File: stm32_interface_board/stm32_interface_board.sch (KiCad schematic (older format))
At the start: 17 parts, among them P1 USB_OTG, P10 CONN_01X03, P11 CONN_01X02, P2 CONN_02X25, P3 CONN_02X25, P4 CONN_01X04, P5 CONN_01X04, P6 CONN_01X04, P7 CONN_01X02, P8 CONN_01X02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

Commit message: Adding build errata to STM32 interface board.
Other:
- note added: "IMPORTANT ERRATA:\nThe connections from P3 pins 25, 27, 29 and 32 are not accurate!!\nThe following modifications were made to the board during assembly:\n\nPin 27 and pin 28 were shorted, as pin 27 is incapable of PWM\nTherefore, pin 28 (i.e. PD6) is to be used for PWM.\n\nPin 30 and pin 32 were shorted, as pin 32 is incapable of PWM\nTherefore, pin 30 (i.e. PD4) is to be used for PWM\n\nPins 25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"
- note added: "STM32 P1"
- note added: "STM32 P2"
- moved on the sheet: C12, C13, U3
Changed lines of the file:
@@
 L +BATT #PWR2
 U 1 1 58BAE894
-P 1500 6050
-F 0 "#PWR2" H 1500 5900 50  0001 C CNN
-F 1 "+BATT" H 1500 6190 50  0000 C CNN
-F 2 "" H 1500 6050 50  0000 C CNN
-F 3 "" H 1500 6050 50  0000 C CNN
-	1    1500 6050
+P 850 7150
+F 0 "#PWR2" H 850 7000 50  0001 C CNN
+F 1 "+BATT" H 850 7290 50  0000 C CNN
+F 2 "" H 850 7150 50  0000 C CNN
+F 3 "" H 850 7150 50  0000 C CNN
+	1    850  7150
 	1    0    0    -1
 $EndComp
@@
 L LF50ABDT-TR U3
 U 1 1 58BB42A6
-P 2750 6150
-F 0 "U3" H 2450 6500 50  0000 L CNN
-F 1 "LF50ABDT-TR" H 2450 6400 50  0000 L CNN
-F 2 "TO_SOT_Packages_SMD:TO-252-2Lead" H 2750 6000 50  0001 L CNN
-F 3 "" H 2750 6300 50  0001 C CNN
-	1    2750 6150
+P 2100 7250
+F 0 "U3" H 1800 7600 50  0000 L CNN
+F 1 "LF50ABDT-TR" H 1800 7500 50  0000 L CNN
+F 2 "TO_SOT_Packages_SMD:TO-252-2Lead" H 2100 7100 50  0001 L CNN
+F 3 "" H 2100 7400 50  0001 C CNN
+	1    2100 7250
 	1    0    0    -1
 $EndComp
@@
 L C C12
 U 1 1 58BB4CB4
-P 1900 6250
-F 0 "C12" H 1925 6350 50  0000 L CNN
-F 1 "0.1 uF" H 1925 6150 50  0000 L CNN
-F 2 "Capacitors_SMD:C_0603_HandSoldering" H 1938 6100 50  0001 C CNN
-F 3 "" H 1900 6250 50  0000 C CNN
-F 4 "CC0603KRX7R8BB104" H 1900 6250 60  0001 C CNN "manf#"
-	1    1900 6250
+P 1250 7350
+F 0 "C12" H 1275 7450 50  0000 L CNN
+F 1 "0.1 uF" H 1275 7250 50  0000 L CNN
+F 2 "Capacitors_SMD:C_0603_HandSoldering" H 1288 7200 50  0001 C CNN
+F 3 "" H 1250 7350 50  0000 C CNN
+F 4 "CC0603KRX7R8BB104" H 1250 7350 60  0001 C CNN "manf#"
+	1    1250 7350
 	1    0    0    -1
 $EndComp
@@
 L Earth #PWR5
 U 1 1 58BB5537
-P 1900 6500
-F 0 "#PWR5" H 1900 6250 50  0001 C CNN
-F 1 "Earth" H 1900 6350 50  0001 C CNN
-F 2 "" H 1900 6500 50  0000 C CNN
-F 3 "" H 1900 6500 50  0000 C CNN
-	1    1900 6500
+P 1250 7600
+F 0 "#PWR5" H 1250 7350 50  0001 C CNN
+F 1 "Earth" H 1250 7450 50  0001 C CNN
+F 2 "" H 1250 7600 50  0000 C CNN
+F 3 "" H 1250 7600 50  0000 C CNN
+	1    1250 7600
 	1    0    0    -1
 $EndComp
@@
 L Earth #PWR8
 U 1 1 58BB56DD
-P 2750 6500
-F 0 "#PWR8" H 2750 6250 50  0001 C CNN
-F 1 "Earth" H 2750 6350 50  0001 C CNN
-F 2 "" H 2750 6500 50  0000 C CNN
-F 3 "" H 2750 6500 50  0000 C CNN
-	1    2750 6500
+P 2100 7600
+F 0 "#PWR8" H 2100 7350 50  0001 C CNN
+F 1 "Earth" H 2100 7450 50  0001 C CNN
+F 2 "" H 2100 7600 50  0000 C CNN
+F 3 "" H 2100 7600 50  0000 C CNN
+	1    2100 7600
 	1    0    0    -1
 $EndComp
@@
 L Earth #PWR9
 U 1 1 58BB5950
-P 3400 6500
-F 0 "#PWR9" H 3400 6250 50  0001 C CNN
-F 1 "Earth" H 3400 6350 50  0001 C CNN
-F 2 "" H 3400 6500 50  0000 C CNN
-F 3 "" H 3400 6500 50  0000 C CNN
-	1    3400 6500
+P 2750 7600
+F 0 "#PWR9" H 2750 7350 50  0001 C CNN
+F 1 "Earth" H 2750 7450 50  0001 C CNN
+F 2 "" H 2750 7600 50  0000 C CNN
+F 3 "" H 2750 7600 50  0000 C CNN
+	1    2750 7600
 	1    0    0    -1
 $EndComp
@@
 L CP C13
 U 1 1 58BB5B23
-P 3400 6200
-F 0 "C13" H 3425 6300 50  0000 L CNN
-F 1 "2.2 uF" H 3425 6100 50  0000 L CNN
-F 2 "Capacitors_ThroughHole:C_Radial_D6.3_L11.2_P2.5" H 3438 6050 50  0001 C CNN
-F 3 "" H 3400 6200 50  0000 C CNN
-	1    3400 6200
+P 2750 7300
+F 0 "C13" H 2775 7400 50  0000 L CNN
+F 1 "2.2 uF" H 2775 7200 50  0000 L CNN
+F 2 "Capacitors_ThroughHole:C_Radial_D6.3_L11.2_P2.5" H 2788 7150 50  0001 C CNN
+F 3 "" H 2750 7300 50  0000 C CNN
+	1    2750 7300
 	1    0    0    -1
 $EndComp
@@
 L +5V #PWR10
 U 1 1 58BB5EB8
-P 3800 6050
-F 0 "#PWR10" H 3800 5900 50  0001 C CNN
-F 1 "+5V" H 3800 6190 50  0000 C CNN
-F 2 "" H 3800 6050 50  0000 C CNN
-F 3 "" H 3800 6050 50  0000 C CNN
-	1    3800 6050
+P 3150 7150
+F 0 "#PWR10" H 3150 7000 50  0001 C CNN
+F 1 "+5V" H 3150 7290 50  0000 C CNN
+F 2 "" H 3150 7150 50  0000 C CNN
+F 3 "" H 3150 7150 50  0000 C CNN
+	1    3150 7150
 	1    0    0    -1
 $EndComp
@@
 L PWR_FLAG #FLG1
 U 1 1 58BBA346
-P 2050 5900
-F 0 "#FLG1" H 2050 5995 50  0001 C CNN
-F 1 "PWR_FLAG" H 2050 6080 50  0000 C CNN
-F 2 "" H 2050 5900 50  0000 C CNN
-F 3 "" H 2050 5900 50  0000 C CNN
-	1    2050 5900
+P 1400 7000
+F 0 "#FLG1" H 1400 7095 50  0001 C CNN
+F 1 "PWR_FLAG" H 1400 7180 50  0000 C CNN
+F 2 "" H 1400 7000 50  0000 C CNN
+F 3 "" H 1400 7000 50  0000 C CNN
+	1    1400 7000
 	1    0    0    -1
 $EndComp
@@
 L PWR_FLAG #FLG2
 U 1 1 58BBD00B
-P 4350 5900
-F 0 "#FLG2" H 4350 5995 50  0001 C CNN
-F 1 "PWR_FLAG" H 4350 6080 50  0000 C CNN
-F 2 "" H 4350 5900 50  0000 C CNN
-F 3 "" H 4350 5900 50  0000 C CNN
-	1    4350 5900
+P 3700 7000
+F 0 "#FLG2" H 3700 7095 50  0001 C CNN
+F 1 "PWR_FLAG" H 3700 7180 50  0000 C CNN
+F 2 "" H 3700 7000 50  0000 C CNN
+F 3 "" H 3700 7000 50  0000 C CNN
+	1    3700 7000
 	1    0    0    -1
 $EndComp
@@
 	5100 4550 5500 4550
 Wire Wire Line
-	1500 6050 2350 6050
-Wire Wire Line
-	1900 6100 1900 6050
-Connection ~ 1900 6050
-Wire Wire Line
-	1900 6500 1900 6400
-Wire Wire Line
-	2750 6500 2750 6350
-Wire Wire Line
-	3150 6050 3800 6050
-Wire Wire Line
-	3400 6350 3400 6500
-Connection ~ 3400 6050
+	850  7150 1700 7150
+Wire Wire Line
+	1250 7200 1250 7150
+Connection ~ 1250 7150
+Wire Wire Line
+	1250 7600 1250 7500
+Wire Wire Line
+	2100 7600 2100 7450
+Wire Wire Line
+	2500 7150 3150 7150
+Wire Wire Line
+	2750 7450 2750 7600
+Connection ~ 2750 7150
 Wire Wire Line
 	7150 4650 7150 4600
@@
 	8800 4050 8800 4250
 Wire Wire Line
-	2050 6050 2050 5900
-Connection ~ 2050 6050
-Wire Wire Line
-	3400 6400 4350 6400
-Wire Wire Line
-	4350 6400 4350 5900
-Connection ~ 3400 6400
+	1400 7150 1400 7000
+Connection ~ 1400 7150
+Wire Wire Line
+	2750 7500 3700 7500
+Wire Wire Line
+	3700 7500 3700 7000
+Connection ~ 2750 7500
 Wire Wire Line
 	4600 3950 4350 3950
@@
 Wire Wire Line
 	1600 1900 1800 1900
+Text Notes 1350 6500 0    60   ~ 0
+IMPORTANT ERRATA:\nThe connections from P3 pins 25, 27, 29 and 32 are not accurate!!\nThe following modifications were made to the board during assembly:\n\nPin 27 and pin 28 were shorted, as pin 27 is incapable of PWM\nTherefore, pin 28 (i.e. PD6) is to be used for PWM.\n\nPin 30 and pin 32 were shorted, as pin 32 is incapable of PWM\nTherefore, pin 30 (i.e. PD4) is to be used for PWM\n\nPins 25 and 29 are PWM-capable and can be used as indicated.\n\nAdditionally, The MCU_TX and MCU_RX lines are routed to PA9 and PA10 respectively. Use those pins for UART!!
+Text Notes 4600 2350 0    60   ~ 0
+STM32 P2
+Text Notes 1400 2350 0    60   ~ 0
+STM32 P1
+Wire Notes Line
+	1300 5250 6600 5250
+Wire Notes Line
+	6600 5250 6600 6550
+Wire Notes Line
+	6600 6550 1300 6550
+Wire Notes Line
+	1300 6550 1300 5250
 $EndSCHEMATC

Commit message: Adding latest STM32 Interface board files.
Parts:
- added TH1, TH2, TH3: PTH, mechanical:PTH, symbol PTH
- C13: manf# (none) -> SN2R2M025ST
- P4, P5, P6: manf# (none) -> PPTC041LFBN-RC
- P7, P8: manf# (none) -> 0705530001
- U3: manf# (none) -> LF50ABDT-TR
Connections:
- net AIN0: now also P2.11 (P11); no longer P3.19 (P19)
- net AIN1: now also P2.14 (P14); no longer P3.20 (P20)
- net ECHO2: now also P2.22 (P22); no longer P3.40 (P40)
- net Earth: now also TH1.1, TH2.1, TH3.1
- net MCU_RX: now also P3.43 (P43); no longer P3.11 (P11)
- net MCU_TX: now also P3.44 (P44); no longer P3.14 (P14)
- net TRIG1: now also P3.34 (P34); no longer P3.41 (P41)
- net TRIG2: now also P2.5 (P5); no longer P3.42 (P42)
- net M1_1: now reaches P3.28 (P28)
- net M2_2: now reaches P3.30 (P30)
- net MotorDriver/M1_PWM1: no longer names the net of P3.27 (P27)
- net MotorDriver/M1_PWM2 renamed M1_2
- net MotorDriver/M2_PWM1 renamed M2_1
- net MotorDriver/M2_PWM2: no longer names the net of P3.32 (P32)
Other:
- note removed: "IMPORTANT ERRATA:\nThe connections from P3 pins 25, 27, 29 and 32 are not accurate!!\nThe following modifications were made to the board during assembly:\n\nPin 27 and pin 28 were shorted, as pin 27 is incapable of PWM\nTherefore, pin 28 (i.e. PD6) is to be used for PWM.\n\nPin 30 and pin 32 were shorted, as pin 32 is incapable of PWM\nTherefore, pin 30 (i.e. PD4) is to be used for PWM\n\nPins 25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"
- note removed: "STM32 P1"
- note removed: "STM32 P2"
- moved on the sheet: C12, C13, U3

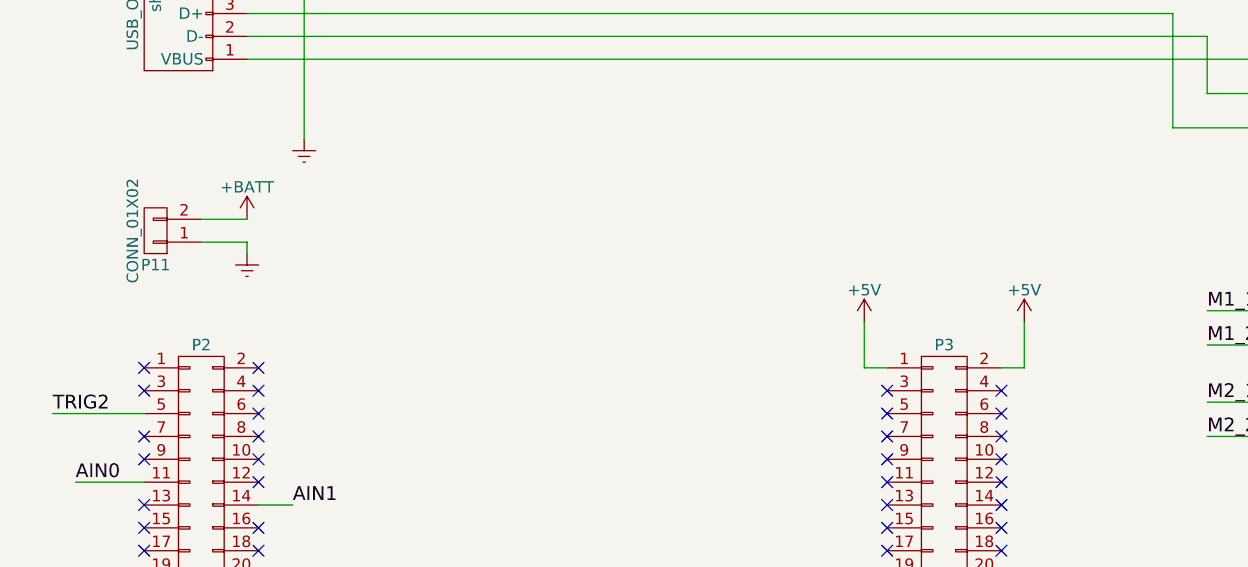
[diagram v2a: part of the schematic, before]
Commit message: Adding latest schematics and clarifications.
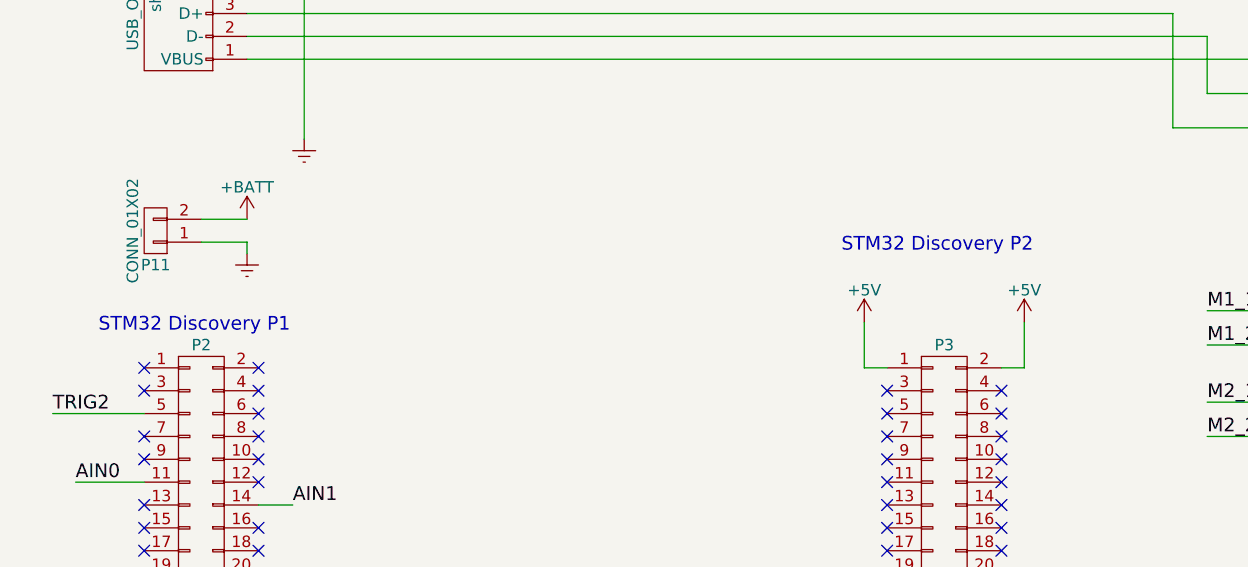
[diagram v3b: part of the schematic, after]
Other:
- note added: "STM32 Discovery P1"
- note added: "STM32 Discovery P2"
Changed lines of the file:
@@
 Sheet 1 3
 Title ""
-Date ""
-Rev ""
+Date "2017-04-05"
+Rev "Release-0.1"
 Comp ""
-Comment1 ""
-Comment2 ""
-Comment3 ""
-Comment4 ""
+Comment1 "STM-F3-IFACE-001"
+Comment2 "STM-F3-IFACE-101"
+Comment3 "Abhimanyu Ghosh"
+Comment4 "Abhimanyu Ghosh"
 $EndDescr
 $Comp
@@
 Wire Wire Line
 	950  2750 1350 2750
+Text Notes 4400 2050 0    60   ~ 0
+STM32 Discovery P2
+Text Notes 1150 2400 0    60   ~ 0
+STM32 Discovery P1
 $EndSCHEMATC

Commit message: Updating STM Interface board to latest rev.
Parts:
- added TH4: PTH, mechanical:PTH, symbol PTH
- P10, P9: manf# (none) -> 61300311021
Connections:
- net +5V: now also P10.3 (P3), P9.3 (P3); no longer P10.2 (P2), P9.2 (P2)
- net ECHO2: now also P3.3 (P3); no longer P2.22 (P22)
- net Earth: now also P10.2 (P2), P9.2 (P2), TH4.1; no longer P10.3 (P3), P9.3 (P3)
- net TRIG2: now also P2.22 (P22); no longer P2.5 (P5)
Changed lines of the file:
@@
 NoConn ~ 1800 900
 $Comp
-L Earth #PWR01
+L Earth #PWR6
 U 1 1 58B8E8C6
 P 2050 1550
-F 0 "#PWR01" H 2050 1300 50  0001 C CNN
+F 0 "#PWR6" H 2050 1300 50  0001 C CNN
 F 1 "Earth" H 2050 1400 50  0001 C CNN
 F 2 "" H 2050 1550 50  0000 C CNN
@@
 $EndComp
 $Comp
-L Earth #PWR02
+L Earth #PWR22
 U 1 1 58B904D9
 P 7650 3700
-F 0 "#PWR02" H 7650 3450 50  0001 C CNN
+F 0 "#PWR22" H 7650 3450 50  0001 C CNN
 F 1 "Earth" H 7650 3550 50  0001 C CNN
 F 2 "" H 7650 3700 50  0000 C CNN
@@
 $EndComp
 $Comp
-L Earth #PWR03
+L Earth #PWR23
 U 1 1 58B9076B
 P 7650 4700
-F 0 "#PWR03" H 7650 4450 50  0001 C CNN
+F 0 "#PWR23" H 7650 4450 50  0001 C CNN
 F 1 "Earth" H 7650 4550 50  0001 C CNN
 F 2 "" H 7650 4700 50  0000 C CNN
@@
 $EndComp
 $Comp
-L Earth #PWR04
+L Earth #PWR24
 U 1 1 58B908A6
 P 7650 5650
-F 0 "#PWR04" H 7650 5400 50  0001 C CNN
+F 0 "#PWR24" H 7650 5400 50  0001 C CNN
 F 1 "Earth" H 7650 5500 50  0001 C CNN
 F 2 "" H 7650 5650 50  0000 C CNN
@@
 MCU_TX
 $Comp
-L Earth #PWR05
+L Earth #PWR12
 U 1 1 58BAD096
 P 4300 5050
-F 0 "#PWR05" H 4300 4800 50  0001 C CNN
+F 0 "#PWR12" H 4300 4800 50  0001 C CNN
 F 1 "Earth" H 4300 4900 50  0001 C CNN
 F 2 "" H 4300 5050 50  0000 C CNN
@@
 $EndComp
 $Comp
-L Earth #PWR06
+L Earth #PWR15
 U 1 1 58BAD1E5
 P 5450 5050
-F 0 "#PWR06" H 5450 4800 50  0001 C CNN
+F 0 "#PWR15" H 5450 4800 50  0001 C CNN
 F 1 "Earth" H 5450 4900 50  0001 C CNN
 F 2 "" H 5450 5050 50  0000 C CNN
@@
 $EndComp
 $Comp
-L Earth #PWR07
+L Earth #PWR7
 U 1 1 58BAD25C
 P 2100 5050
-F 0 "#PWR07" H 2100 4800 50  0001 C CNN
+F 0 "#PWR7" H 2100 4800 50  0001 C CNN
 F 1 "Earth" H 2100 4900 50  0001 C CNN
 F 2 "" H 2100 5050 50  0000 C CNN
@@
 $EndComp
 $Comp
-L Earth #PWR08
+L Earth #PWR1
 U 1 1 58BAD304
 P 1050 5050
-F 0 "#PWR08" H 1050 4800 50  0001 C CNN
+F 0 "#PWR1" H 1050 4800 50  0001 C CNN
 F 1 "Earth" H 1050 4900 50  0001 C CNN
 F 2 "" H 1050 5050 50  0000 C CNN
@@
 NoConn ~ 1850 2550
 $Comp
-L +BATT #PWR09
+L +BATT #PWR2
 U 1 1 58BAE894
 P 1500 6050
-F 0 "#PWR09" H 1500 5900 50  0001 C CNN
+F 0 "#PWR2" H 1500 5900 50  0001 C CNN
 F 1 "+BATT" H 1500 6190 50  0000 C CNN
 F 2 "" H 1500 6050 50  0000 C CNN
@@
 $EndComp
 $Comp
-L +5V #PWR010
+L +5V #PWR13
 U 1 1 58BAEE3E
 P 4500 2350
-F 0 "#PWR010" H 4500 2200 50  0001 C CNN
+F 0 "#PWR13" H 4500 2200 50  0001 C CNN
 F 1 "+5V" H 4500 2490 50  0000 C CNN
 F 2 "" H 4500 2350 50  0000 C CNN
@@
 $EndComp
 $Comp
-L +5V #PWR011
+L +5V #PWR14
 U 1 1 58BAEEBC
 P 5200 2350
-F 0 "#PWR011" H 5200 2200 50  0001 C CNN
+F 0 "#PWR14" H 5200 2200 50  0001 C CNN
 F 1 "+5V" H 5200 2490 50  0000 C CNN
 F 2 "" H 5200 2350 50  0000 C CNN
@@
 $EndComp
 $Comp
-L +5V #PWR012
+L +5V #PWR16
 U 1 1 58BAF3C8
 P 7000 3650
-F 0 "#PWR012" H 7000 3500 50  0001 C CNN
+F 0 "#PWR16" H 7000 3500 50  0001 C CNN
 F 1 "+5V" H 7000 3790 50  0000 C CNN
 F 2 "" H 7000 3650 50  0000 C CNN
@@
 $EndComp
 $Comp
-L +5V #PWR013
+L +5V #PWR17
 U 1 1 58BAF4B7
 P 7000 4600
-F 0 "#PWR013" H 7000 4450 50  0001 C CNN
+F 0 "#PWR17" H 7000 4450 50  0001 C CNN
 F 1 "+5V" H 7000 4740 50  0000 C CNN
 F 2 "" H 7000 4600 50  0000 C CNN
@@
 $EndComp
 $Comp
-L +5V #PWR014
+L +5V #PWR18
 U 1 1 58BAF5A7
 P 7000 5550
-F 0 "#PWR014" H 7000 5400 50  0001 C CNN
+F 0 "#PWR18" H 7000 5400 50  0001 C CNN
 F 1 "+5V" H 7000 5690 50  0000 C CNN
 F 2 "" H 7000 5550 50  0000 C CNN
@@
 $EndComp
 $Comp
-L Earth #PWR015
+L Earth #PWR28
 U 1 1 58B90A89
 P 9300 4450
-F 0 "#PWR015" H 9300 4200 50  0001 C CNN
+F 0 "#PWR28" H 9300 4200 50  0001 C CNN
 F 1 "Earth" H 9300 4300 50  0001 C CNN
 F 2 "" H 9300 4450 50  0000 C CNN
@@
 $EndComp
 $Comp
-L Earth #PWR016
+L Earth #PWR27
 U 1 1 58B9091D
 P 9300 3900
-F 0 "#PWR016" H 9300 3650 50  0001 C CNN
+F 0 "#PWR27" H 9300 3650 50  0001 C CNN
 F 1 "Earth" H 9300 3750 50  0001 C CNN
 F 2 "" H 9300 3900 50  0000 C CNN
@@
 F 2 "Pin_Headers:Pin_Header_Straight_1x03" H 9700 3700 50  0001 C CNN
 F 3 "" H 9700 3700 50  0000 C CNN
+F 4 "61300311021" H 9700 3700 60  0001 C CNN "manf#"
 	1    9700 3700
 	1    0    0    -1
@@
 Text Label 3900 4450 0    60   ~ 0
 ECHO1
-Text Label 2000 3550 0    60   ~ 0
+Text Label 4150 2650 0    60   ~ 0
 ECHO2
 Text Label 7200 3450 0    60   ~ 0
@@
 Text Label 5250 4150 0    60   ~ 0
 TRIG1
-Text Label 950  2750 0    60   ~ 0
+Text Label 2000 3550 0    60   ~ 0
 TRIG2
 $Comp
@@
 $EndComp
 $Comp
-L Earth #PWR017
+L Earth #PWR5
 U 1 1 58BB5537
 P 1900 6500
-F 0 "#PWR017" H 1900 6250 50  0001 C CNN
+F 0 "#PWR5" H 1900 6250 50  0001 C CNN
 F 1 "Earth" H 1900 6350 50  0001 C CNN
 F 2 "" H 1900 6500 50  0000 C CNN
@@
 $EndComp
 $Comp
-L Earth #PWR018
+L Earth #PWR9
 U 1 1 58BB56DD
 P 2750 6500
-F 0 "#PWR018" H 2750 6250 50  0001 C CNN
+F 0 "#PWR9" H 2750 6250 50  0001 C CNN
 F 1 "Earth" H 2750 6350 50  0001 C CNN
 F 2 "" H 2750 6500 50  0000 C CNN
@@
 $EndComp
 $Comp
-L Earth #PWR019
+L Earth #PWR10
 U 1 1 58BB5950
 P 3400 6500
-F 0 "#PWR019" H 3400 6250 50  0001 C CNN
+F 0 "#PWR10" H 3400 6250 50  0001 C CNN
 F 1 "Earth" H 3400 6350 50  0001 C CNN
 F 2 "" H 3400 6500 50  0000 C CNN
@@
 $EndComp
 $Comp
-L +5V #PWR020
+L +5V #PWR11
 U 1 1 58BB5EB8
 P 3800 6050
-F 0 "#PWR020" H 3800 5900 50  0001 C CNN
+F 0 "#PWR11" H 3800 5900 50  0001 C CNN
 F 1 "+5V" H 3800 6190 50  0000 C CNN
 F 2 "" H 3800 6050 50  0000 C CNN
@@
 $EndComp
 $Comp
-L Earth #PWR021
+L Earth #PWR19
 U 1 1 58BB8CAA
 P 7150 4050
-F 0 "#PWR021" H 7150 3800 50  0001 C CNN
+F 0 "#PWR19" H 7150 3800 50  0001 C CNN
 F 1 "Earth" H 7150 3900 50  0001 C CNN
 F 2 "" H 7150 4050 50  0000 C CNN
@@
 $EndComp
 $Comp
-L Earth #PWR022
+L Earth #PWR20
 U 1 1 58BB8D33
 P 7150 5000
-F 0 "#PWR022" H 7150 4750 50  0001 C CNN
+F 0 "#PWR20" H 7150 4750 50  0001 C CNN
 F 1 "Earth" H 7150 4850 50  0001 C CNN
 F 2 "" H 7150 5000 50  0000 C CNN
@@
 $EndComp
 $Comp
-L Earth #PWR023
+L Earth #PWR21
 U 1 1 58BB8DBC
 P 7150 5950
-F 0 "#PWR023" H 7150 5700 50  0001 C CNN
+F 0 "#PWR21" H 7150 5700 50  0001 C CNN
 F 1 "Earth" H 7150 5800 50  0001 C CNN
 F 2 "" H 7150 5950 50  0000 C CNN
@@
 $EndComp
 $Comp
-L +5V #PWR024
+L +5V #PWR25
 U 1 1 58BB997C
 P 8800 3550
-F 0 "#PWR024" H 8800 3400 50  0001 C CNN
+F 0 "#PWR25" H 8800 3400 50  0001 C CNN
 F 1 "+5V" H 8800 3690 50  0000 C CNN
 F 2 "" H 8800 3550 50  0000 C CNN
@@
 $EndComp
 $Comp
-L +5V #PWR025
+L +5V #PWR26
 U 1 1 58BB9B9D
 P 8800 4050
-F 0 "#PWR025" H 8800 3900 50  0001 C CNN
+F 0 "#PWR26" H 8800 3900 50  0001 C CNN
 F 1 "+5V" H 8800 4190 50  0000 C CNN
 F 2 "" H 8800 4050 50  0000 C CNN
@@
 $EndComp
 $Comp
-L PWR_FLAG #FLG026
+L PWR_FLAG #FLG1
 U 1 1 58BBA346
 P 2050 5900
-F 0 "#FLG026" H 2050 5995 50  0001 C CNN
+F 0 "#FLG1" H 2050 5995 50  0001 C CNN
 F 1 "PWR_FLAG" H 2050 6080 50  0000 C CNN
 F 2 "" H 2050 5900 50  0000 C CNN
@@
 NoConn ~ 4600 2750
 NoConn ~ 5100 2750
-NoConn ~ 4600 2650
 NoConn ~ 5100 2650
 $Comp
-L PWR_FLAG #FLG027
+L PWR_FLAG #FLG2
 U 1 1 58BBD00B
 P 4350 5900
-F 0 "#FLG027" H 4350 5995 50  0001 C CNN
+F 0 "#FLG2" H 4350 5995 50  0001 C CNN
 F 1 "PWR_FLAG" H 4350 6080 50  0000 C CNN
 F 2 "" H 4350 5900 50  0000 C CNN
@@
 F 2 "Pin_Headers:Pin_Header_Straight_1x03" H 9700 4250 50  0001 C CNN
 F 3 "" H 9700 4250 50  0000 C CNN
+F 4 "61300311021" H 9700 4250 60  0001 C CNN "manf#"
 	1    9700 4250
 	1    0    0    -1
@@
 	7000 5550 7850 5550
 Wire Wire Line
-	8800 3700 9500 3700
-Wire Wire Line
-	8800 4250 9500 4250
-Wire Wire Line
-	9300 3800 9500 3800
-Wire Wire Line
-	9300 3900 9300 3800
-Wire Wire Line
-	9300 4350 9500 4350
-Wire Wire Line
-	9300 4450 9300 4350
+	9300 3700 9300 3900
 Wire Wire Line
 	9000 4150 9500 4150
@@
 	7150 4050 7150 4000
 Wire Wire Line
-	8800 3550 8800 3700
-Wire Wire Line
-	8800 4050 8800 4250
+	8800 3550 8800 3800
+Wire Wire Line
+	8800 4050 8800 4350
 Wire Wire Line
 	2050 6050 2050 5900
@@
 $EndComp
 $Comp
-L +BATT #PWR028
+L +BATT #PWR3
 U 1 1 58D04FAA
 P 1800 1900
-F 0 "#PWR028" H 1800 1750 50  0001 C CNN
+F 0 "#PWR3" H 1800 1750 50  0001 C CNN
 F 1 "+BATT" H 1800 2040 50  0000 C CNN
 F 2 "" H 1800 1900 50  0000 C CNN
@@
 $EndComp
 $Comp
-L Earth #PWR029
+L Earth #PWR4
 U 1 1 58D051BE
 P 1800 2050
-F 0 "#PWR029" H 1800 1800 50  0001 C CNN
+F 0 "#PWR4" H 1800 1800 50  0001 C CNN
 F 1 "Earth" H 1800 1900 50  0001 C CNN
 F 2 "" H 1800 2050 50  0000 C CNN
@@
 $EndComp
 $Comp
-L Earth #PWR030
+L Earth #PWR8
 U 1 1 58DCFA0F
 P 2650 7350
-F 0 "#PWR030" H 2650 7100 50  0001 C CNN
+F 0 "#PWR8" H 2650 7100 50  0001 C CNN
 F 1 "Earth" H 2650 7200 50  0001 C CNN
 F 2 "" H 2650 7350 50  0000 C CNN
@@
 $EndComp
 Wire Wire Line
-	1300 7350 2650 7350
-Wire Wire Line
 	2650 7350 2650 7050
 Wire Wire Line
@@
 	1300 7050 2650 7050
 Wire Wire Line
-	2100 7050 2100 6850
+	2100 6850 2100 7550
 Connection ~ 2100 7050
 $Comp
@@
 Wire Wire Line
 	1850 3550 2000 3550
-Wire Wire Line
-	950  2750 1350 2750
 Text Notes 4400 2050 0    60   ~ 0
 STM32 Discovery P2
 Text Notes 1150 2400 0    60   ~ 0
 STM32 Discovery P1
+NoConn ~ 1350 2750
+Wire Wire Line
+	4150 2650 4600 2650
+$Comp
+L PTH TH4
+U 1 1 58E62AF3
+P 1900 7350
+F 0 "TH4" H 1700 7250 60  0000 C CNN
+F 1 "PTH" H 1700 7500 60  0000 C CNN
+F 2 "mechanical:PTH" H 1900 7350 60  0001 C CNN
+F 3 "" H 1900 7350 60  0000 C CNN
+	1    1900 7350
+	1    0    0    -1
+$EndComp
+Wire Wire Line
+	1300 7350 1300 7550
+Wire Wire Line
+	1300 7550 2100 7550
+Connection ~ 2100 7350
+Wire Wire Line
+	9300 3700 9500 3700
+Wire Wire Line
+	8800 3800 9500 3800
+Wire Wire Line
+	8800 4350 9500 4350
+Wire Wire Line
+	9300 4250 9300 4450
+Wire Wire Line
+	9300 4250 9500 4250
 $EndSCHEMATC
